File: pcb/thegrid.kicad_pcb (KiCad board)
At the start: 2 copper layers, 50 x 50 mm, 46 parts, among them P1 CONN_2, P10 CONN_2, P2 CONN_2, P4 CONN_2, P5 CONN_2, P6 SHIFT_IN, P7 CONN_2, P8 SHIFT_OUT, P9 CONN_2, Q1 FQP7P06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

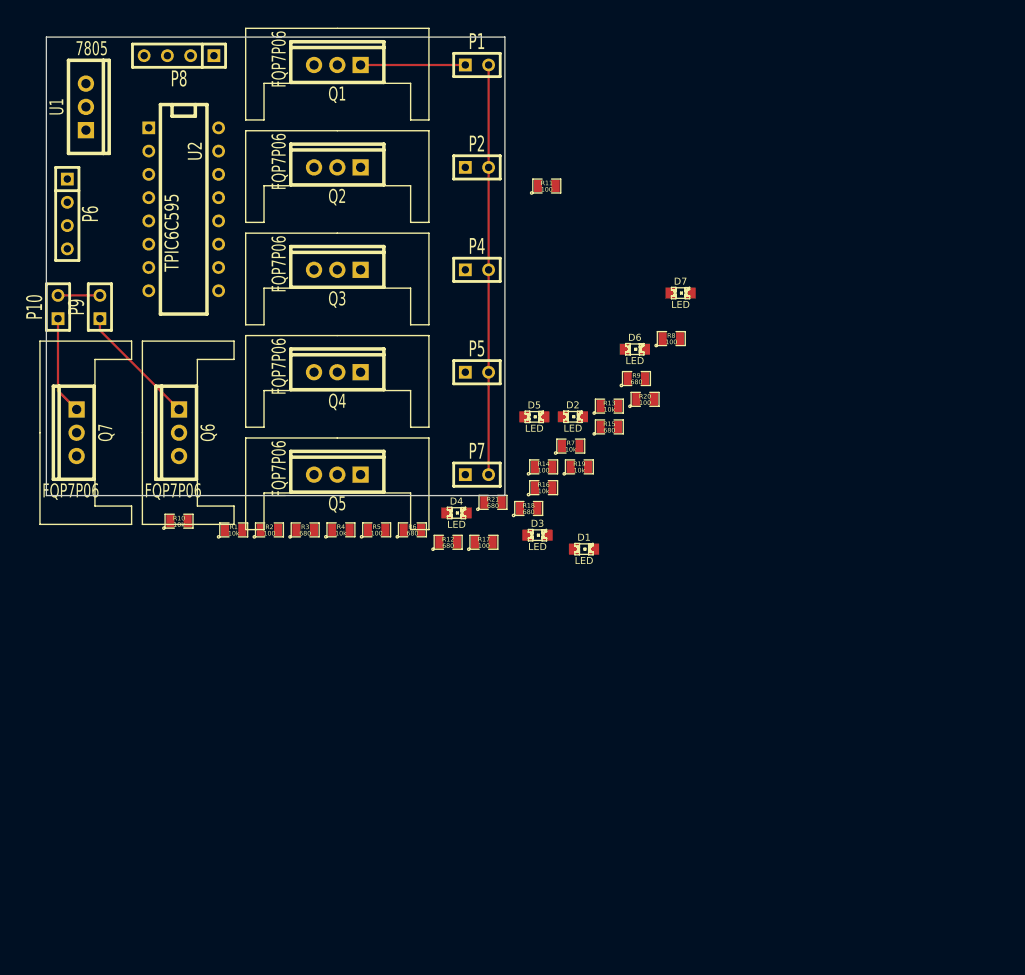
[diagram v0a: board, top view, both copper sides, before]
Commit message: 10cm x 5cm spacey PCB layout
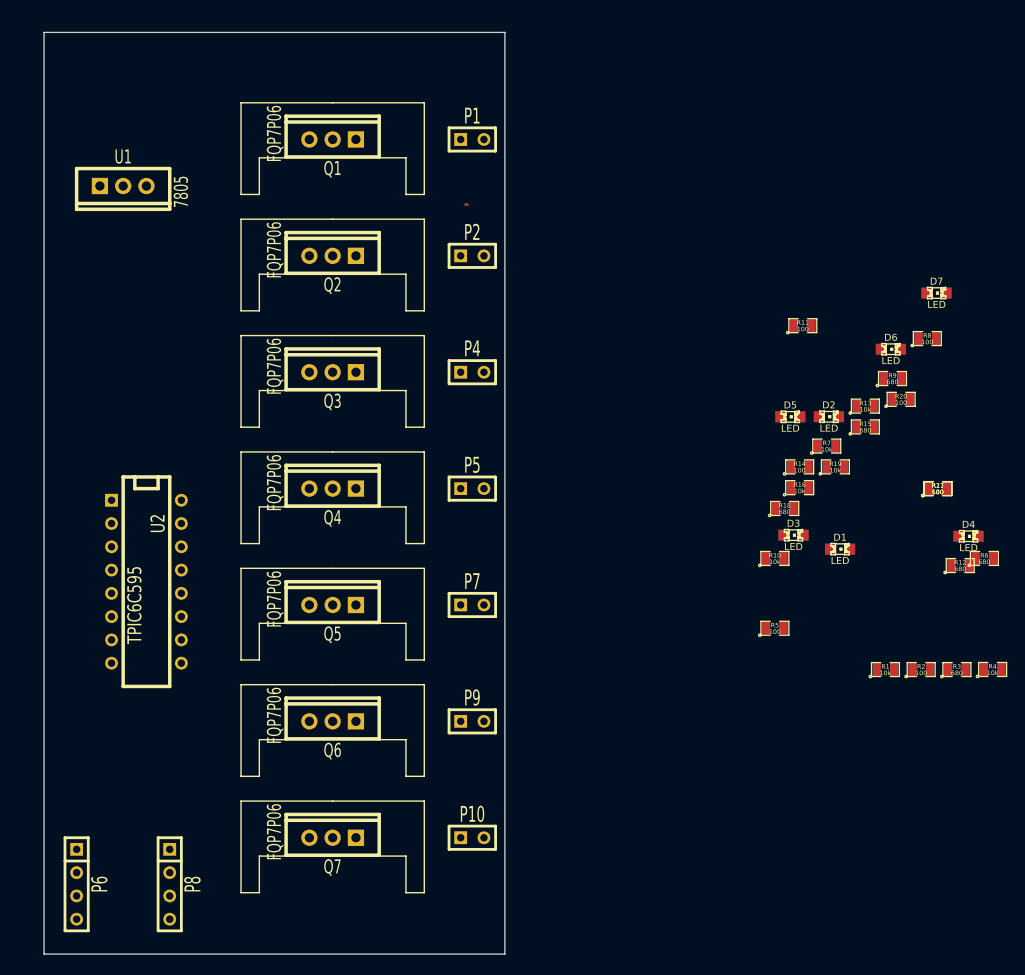
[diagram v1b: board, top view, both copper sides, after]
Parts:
- moved P8 90.4 mm to (134.6, 111.8), turned to 270 degrees
- moved P10 73.5 mm to (167.6, 106.7), turned to 0 degrees
- moved P6 73.2 mm to (124.5, 111.8)
- moved R1 72.7 mm to (212.7, 88.3)
- moved R2 72.7 mm to (216.6, 88.3)
- moved R3 72.7 mm to (220.5, 88.3)
- moved R4 72.7 mm to (224.4, 88.3)
- moved R10 65.2 mm to (200.7, 76.2)
- moved R6 62.5 mm to (223.5, 76.2)
- moved P9 60.8 mm to (167.6, 94.0), turned to 0 degrees
- moved D4 55.9 mm to (221.8, 73.8)
- moved R12 55.9 mm to (220.9, 77.0)
- moved Q7 52.3 mm to (152.4, 106.7), turned to 90 degrees
- moved R17 49.9 mm to (218.4, 68.6)
- moved R21 48.6 mm to (218.4, 68.6)
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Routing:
- net GND: track 49.3 -> 0.00 mm
- net Net-(P9-Pad1): track 13.5 -> 0.00 mm
- net Net-(P1-Pad1): track 11.9 -> 0.00 mm
- net Net-(P10-Pad1): track 10.7 -> 0.00 mm
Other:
- board size 50 x 50 mm -> 50.3 x 100.6 mm

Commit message: All SMD parts to PTH
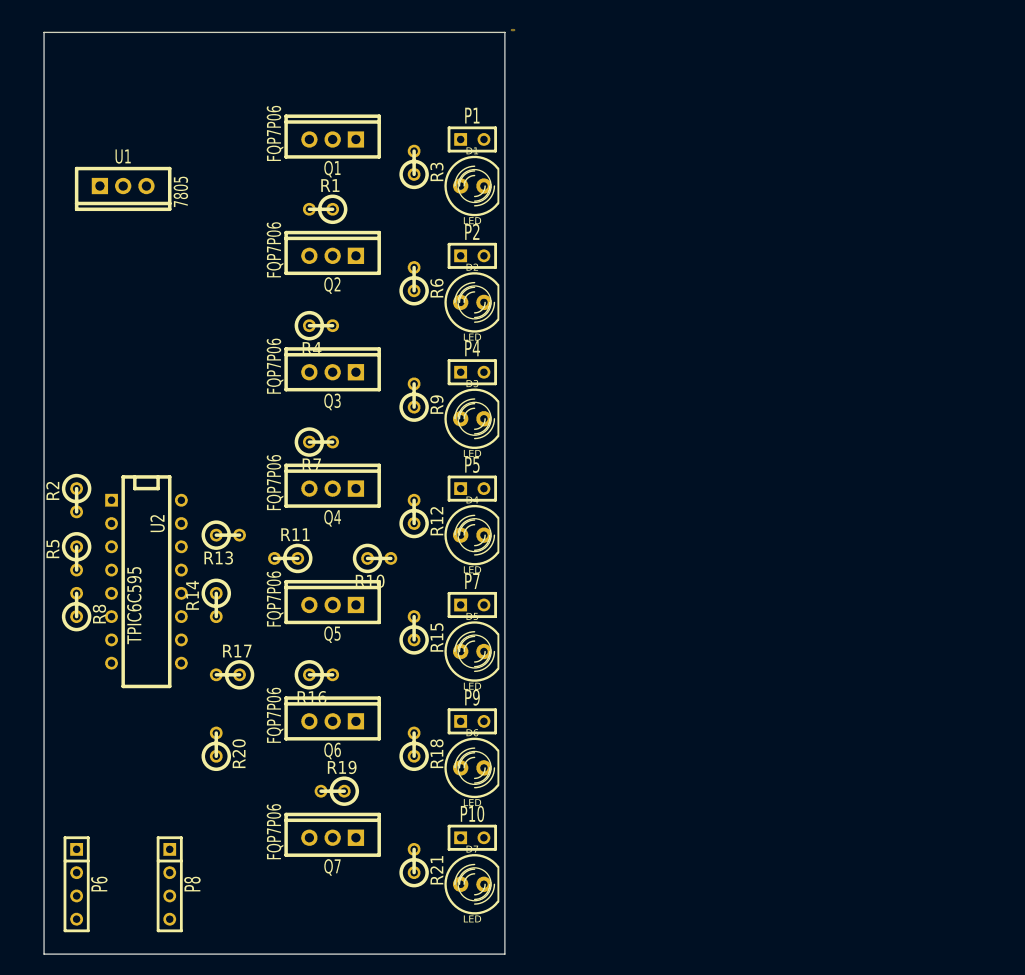
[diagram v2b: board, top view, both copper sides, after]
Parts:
- D1, D2, D3, D4, D5, D6, D7: footprint LEDs:LED-0805 -> LEDs:LED-5MM
- Q1, Q2, Q3, Q4, Q5, Q6, Q7: footprint TO220_hs:TO220_VERT -> Discret:TO220_VERT
- R1, R10, R11, R12, R13, R14, R15, R16, R17, R18, R19, R2, R20, R21, R3, R4, R5, R6, R7, R8, R9: footprint SMD_Packages:SM0805 -> Discret:R1
- moved R8 97.3 mm to (124.5, 81.3), turned to 90 degrees
- moved R2 94.0 mm to (124.5, 69.8), turned to 270 degrees
- moved R20 83.7 mm to (139.7, 96.5), turned to 90 degrees
- moved R4 82.3 mm to (151.1, 50.8)
- moved D7 82.0 mm to (167.6, 111.8)
- moved R3 81.0 mm to (161.3, 33.0), turned to 90 degrees
- moved R17 80.1 mm to (141.0, 88.9), turned to 180 degrees
- moved R1 79.5 mm to (151.1, 38.1), turned to 180 degrees
- moved R5 76.6 mm to (124.5, 76.2), turned to 270 degrees
- moved R13 71.0 mm to (141.0, 73.7)
- moved R21 70.1 mm to (161.3, 109.2), turned to 90 degrees
- moved R6 69.3 mm to (161.3, 45.7), turned to 90 degrees
- moved R14 65.4 mm to (139.7, 81.3), turned to 270 degrees
- moved R19 65.3 mm to (152.4, 101.6), turned to 180 degrees
- moved D6 64.6 mm to (167.6, 99.1)
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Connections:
- U2 pad 14: Net-(U2-Pad14) -> (no net)

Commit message: Changed TO220 to hs again and moved resistors
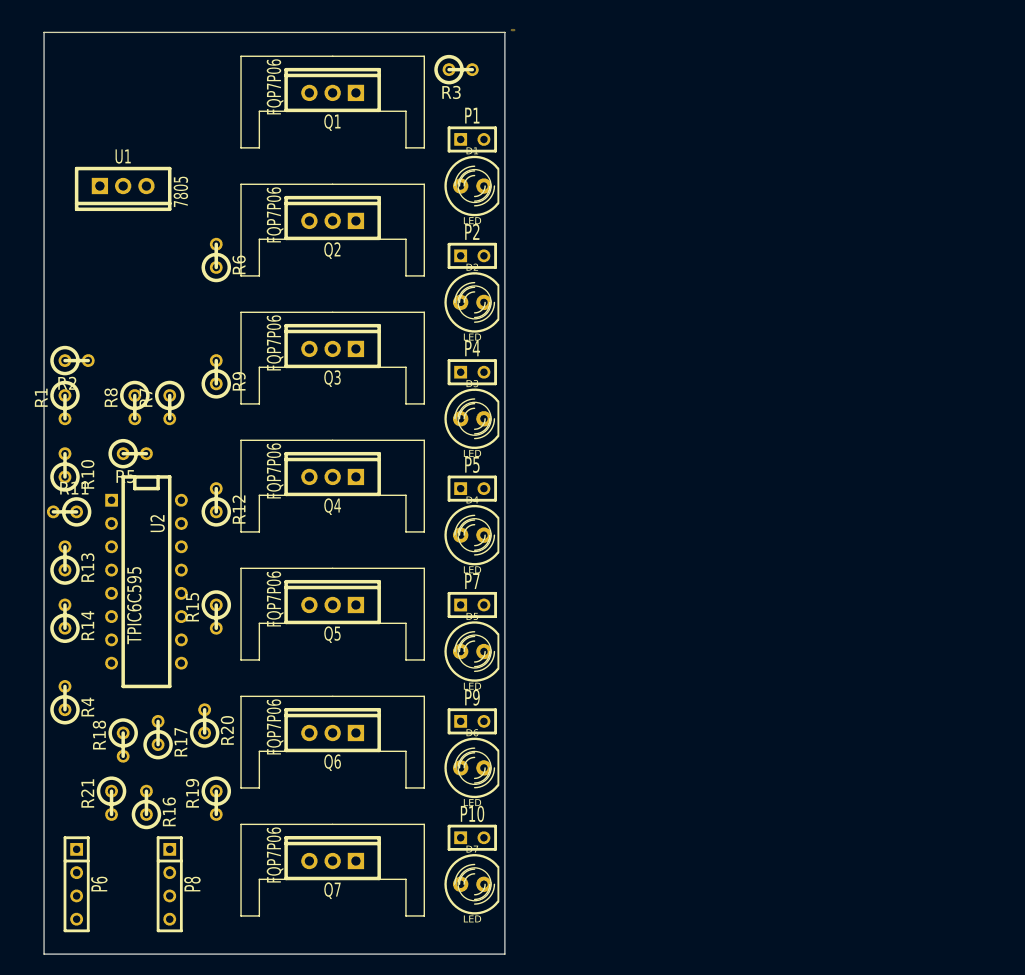
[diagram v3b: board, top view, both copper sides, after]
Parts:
- Q1, Q2, Q3, Q4, Q5, Q6, Q7: footprint Discret:TO220_VERT -> TO220_hs:TO220_VERT
- moved R4 49.3 mm to (123.2, 91.4), turned to 90 degrees
- moved R10 35.8 mm to (123.2, 66.0), turned to 90 degrees
- moved R1 35.3 mm to (123.2, 59.7), turned to 270 degrees
- moved R21 33.6 mm to (128.3, 102.9), turned to 270 degrees
- moved R18 31.8 mm to (129.5, 96.5), turned to 270 degrees
- moved R11 24.7 mm to (123.2, 71.1)
- moved R16 23.6 mm to (132.1, 102.9), turned to 90 degrees
- moved R8 22.5 mm to (130.8, 59.7), turned to 270 degrees
- moved R6 21.7 mm to (139.7, 43.2)
- moved R9 21.7 mm to (139.7, 55.9)
- moved R12 21.6 mm to (139.7, 69.8)
- moved R15 21.6 mm to (139.7, 82.5), turned to 270 degrees
- moved R13 18.0 mm to (123.2, 76.2), turned to 90 degrees
- moved R7 16.9 mm to (134.6, 59.7), turned to 270 degrees
- moved R14 16.6 mm to (123.2, 82.5), turned to 90 degrees
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
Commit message: Schematic touchups and PCB footprint layout
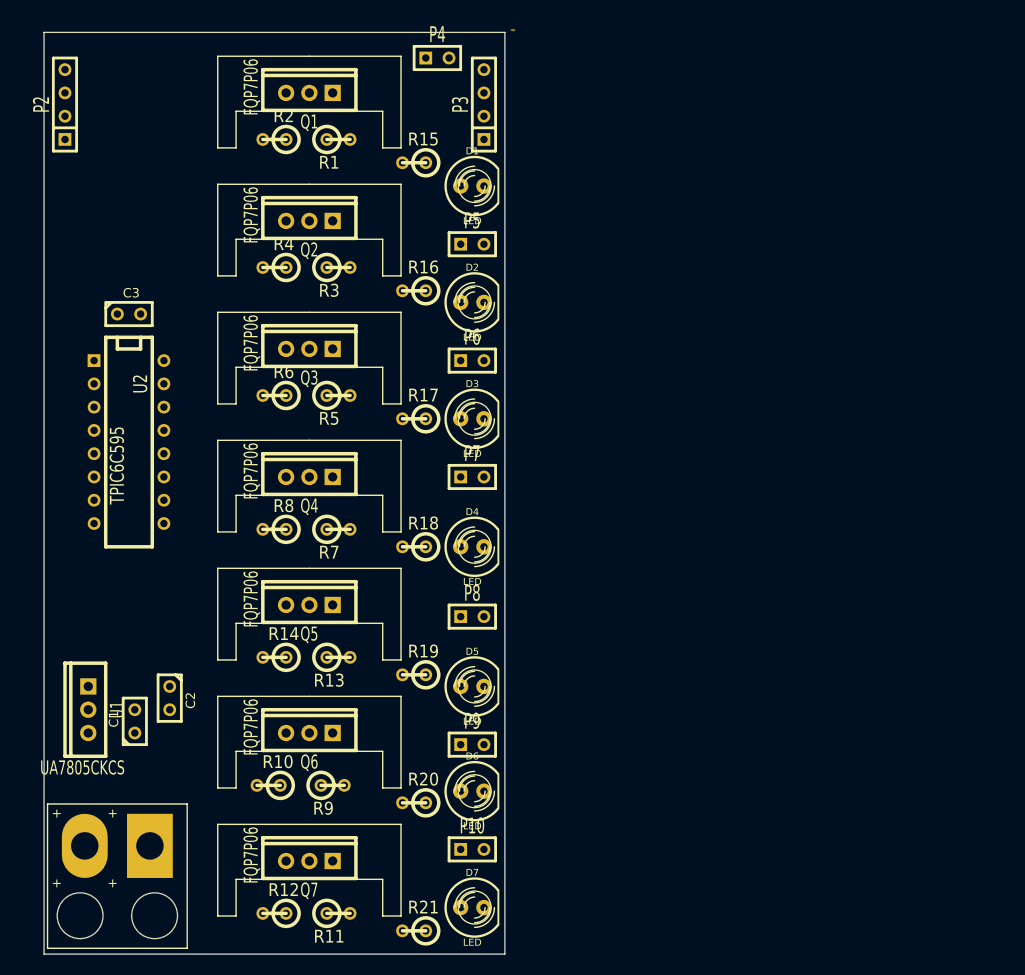
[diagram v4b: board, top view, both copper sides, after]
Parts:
- added C1: .33u, Discret:C1, F.Cu at (130.8, 94.0)
- added C2: .1u, Discret:C1, F.Cu at (134.6, 91.4)
- added C3: 100n, Discret:C1, F.Cu at (130.2, 49.5)
- added P3: SHIFT_OUT, Connect:SIL-4, F.Cu at (168.9, 26.7)
- P1: value CONN_2 -> POWER; footprint Connect:SIL-2 -> solder_pad:SIL-2
- P2: value CONN_2 -> SHIFT_IN; footprint Connect:SIL-2 -> Connect:SIL-4
- P6: value SHIFT_IN -> CONN_2; footprint Connect:SIL-4 -> Connect:SIL-2
- P8: value SHIFT_OUT -> CONN_2; footprint Connect:SIL-4 -> Connect:SIL-2
- R10, R4: value 10k -> 100
- R11, R5: value 100 -> 10k
- R12, R6: value 680 -> 100
- R16, R19: value 10k -> 680
- R17, R20: value 100 -> 680
- R3, R9: value 680 -> 10k
- U1: value 7805 -> UA7805CKCS
- moved P1 87.2 mm to (128.9, 108.6), turned to 180 degrees
- moved P6 71.6 mm to (167.6, 54.6), turned to 0 degrees
- moved R16 63.1 mm to (161.3, 47.0), turned to 180 degrees
- moved U1 57.3 mm to (125.7, 92.7), turned to 180 degrees
- moved R15 54.0 mm to (161.3, 33.0), turned to 180 degrees
- moved R11 53.0 mm to (153.0, 114.9), turned to 0 degrees
- moved R4 52.3 mm to (146.1, 44.5), turned to 180 degrees
- moved P2 47.4 mm to (123.2, 26.7), turned to 90 degrees
- moved R9 46.8 mm to (152.4, 101.0), turned to 0 degrees
- moved R12 45.5 mm to (146.1, 114.9), turned to 180 degrees
- moved R17 44.2 mm to (161.3, 61.0), turned to 180 degrees
- moved P8 44.1 mm to (167.6, 82.5), turned to 0 degrees
- moved R1 41.8 mm to (153.0, 30.5), turned to 0 degrees
- moved R10 41.4 mm to (145.4, 101.0), turned to 180 degrees
- moved R18 38.4 mm to (161.3, 74.9), turned to 180 degrees
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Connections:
- P1 pad 1: Net-(P1-Pad1) -> GND
- P1 pad 2: GND -> +12V
- P2 pad 1: Net-(P2-Pad1) -> GND
- P2 pad 2: GND -> Net-(P2-Pad2)
- P6 pad 1: GND -> Net-(P6-Pad1)
- P6 pad 2: Net-(P6-Pad2) -> GND
- P8 pad 1: GND -> Net-(P8-Pad1)
- P8 pad 2: Net-(P6-Pad2) -> GND
- Q1 pad 1: Net-(P1-Pad1) -> +12V
- Q1 pad 3: +12V -> Net-(P4-Pad1)
- Q2 pad 1: Net-(P2-Pad1) -> +12V
- Q2 pad 3: +12V -> Net-(P5-Pad1)
- Q3 pad 1: Net-(P4-Pad1) -> +12V
- Q3 pad 3: +12V -> Net-(P6-Pad1)
- Q4 pad 1: Net-(P5-Pad1) -> +12V
- Q4 pad 3: +12V -> Net-(P7-Pad1)
- Q5 pad 1: Net-(P7-Pad1) -> +12V
- Q5 pad 3: +12V -> Net-(P8-Pad1)
- Q6 pad 1: Net-(P9-Pad1) -> +12V
- Q6 pad 3: +12V -> Net-(P9-Pad1)
- Q7 pad 1: Net-(P10-Pad1) -> +12V
- Q7 pad 3: +12V -> Net-(P10-Pad1)
- R10 pad 1: Net-(Q4-Pad2) -> Net-(Q6-Pad2)
- R10 pad 2: +12V -> Net-(R10-Pad2)
- R11 pad 1: Net-(Q4-Pad2) -> Net-(Q7-Pad2)
- R11 pad 2: Net-(R11-Pad2) -> +12V
- R12 pad 1: Net-(D4-Pad1) -> Net-(Q7-Pad2)
- R12 pad 2: Net-(P5-Pad1) -> Net-(R12-Pad2)
- R15 pad 1: Net-(D5-Pad1) -> Net-(D1-Pad1)
- R15 pad 2: Net-(P7-Pad1) -> Net-(P4-Pad1)
- R16 pad 1: Net-(Q6-Pad2) -> Net-(D2-Pad1)
- R16 pad 2: +12V -> Net-(P5-Pad1)
- R17 pad 1: Net-(Q6-Pad2) -> Net-(D3-Pad1)
- R17 pad 2: Net-(R17-Pad2) -> Net-(P6-Pad1)
- R18 pad 1: Net-(D6-Pad1) -> Net-(D4-Pad1)
- R18 pad 2: Net-(P9-Pad1) -> Net-(P7-Pad1)
- R19 pad 1: Net-(Q7-Pad2) -> Net-(D5-Pad1)
- R19 pad 2: +12V -> Net-(P8-Pad1)
- R20 pad 1: Net-(Q7-Pad2) -> Net-(D6-Pad1)
- R20 pad 2: Net-(R20-Pad2) -> Net-(P9-Pad1)
- R3 pad 1: Net-(D1-Pad1) -> Net-(Q2-Pad2)
- R3 pad 2: Net-(P1-Pad1) -> +12V
- R4 pad 2: +12V -> Net-(R4-Pad2)
- R5 pad 1: Net-(Q2-Pad2) -> Net-(Q3-Pad2)
- R5 pad 2: Net-(R5-Pad2) -> +12V
- R6 pad 1: Net-(D2-Pad1) -> Net-(Q3-Pad2)
- R6 pad 2: Net-(P2-Pad1) -> Net-(R6-Pad2)
- R7 pad 1: Net-(Q3-Pad2) -> Net-(Q4-Pad2)
- R8 pad 1: Net-(Q3-Pad2) -> Net-(Q4-Pad2)
- R9 pad 1: Net-(D3-Pad1) -> Net-(Q6-Pad2)
- R9 pad 2: Net-(P4-Pad1) -> +12V
- U2 pad 10: Net-(P6-Pad2) -> Net-(P2-Pad2)
- U2 pad 12: Net-(R17-Pad2) -> Net-(R10-Pad2)
- U2 pad 13: Net-(R20-Pad2) -> Net-(R12-Pad2)
- U2 pad 15: Net-(P6-Pad3) -> Net-(P2-Pad3)
- U2 pad 2: Net-(P6-Pad4) -> Net-(P2-Pad4)
- U2 pad 4: Net-(R5-Pad2) -> Net-(R4-Pad2)
- U2 pad 5: Net-(R8-Pad2) -> Net-(R6-Pad2)
- U2 pad 6: Net-(R11-Pad2) -> Net-(R8-Pad2)
- U2 pad 9: Net-(P8-Pad4) -> Net-(P3-Pad4)

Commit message: propower minipower led strip connectors
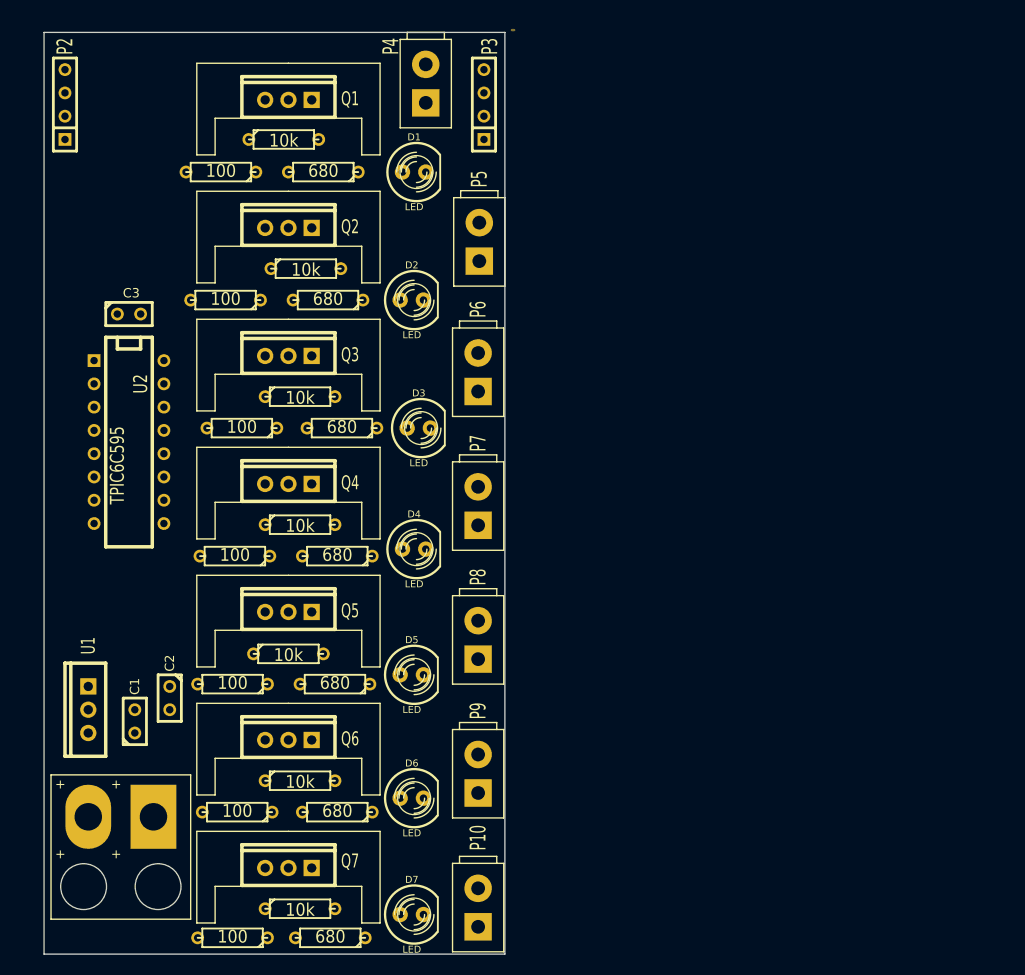
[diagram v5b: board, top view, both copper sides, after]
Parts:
- P10, P4, P5, P6, P7, P8, P9: footprint Connect:SIL-2 -> minipower:SIL-2
- R1, R10, R11, R12, R13, R14, R15, R16, R17, R18, R19, R2, R20, R21, R3, R4, R5, R6, R7, R8, R9: footprint Discret:R1 -> Discret:R3
- moved R15 9.96 mm to (151.4, 34.0)
- moved R16 9.45 mm to (151.9, 48.0)
- moved R21 9.18 mm to (152.1, 117.6)
- moved R19 8.70 mm to (152.7, 89.9)
- moved R18 8.44 mm to (152.9, 75.9)
- moved R20 8.44 mm to (152.9, 103.9)
- moved R17 7.94 mm to (153.4, 62.0)
- moved R2 6.84 mm to (140.2, 34.0)
- moved D5 6.73 mm to (161.0, 88.9)
- moved D6 6.65 mm to (161.0, 102.4)
- moved D7 6.65 mm to (161.0, 115.1)
- moved D2 6.61 mm to (161.0, 48.0)
- moved D1 6.53 mm to (161.3, 34.0)
- moved R4 6.41 mm to (140.7, 48.0)
- moved P10 6.38 mm to (168.3, 114.3), turned to 90 degrees
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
